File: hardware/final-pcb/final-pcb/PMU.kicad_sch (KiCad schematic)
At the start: 1 part, among them U3 LTC3556EUFD-PBF

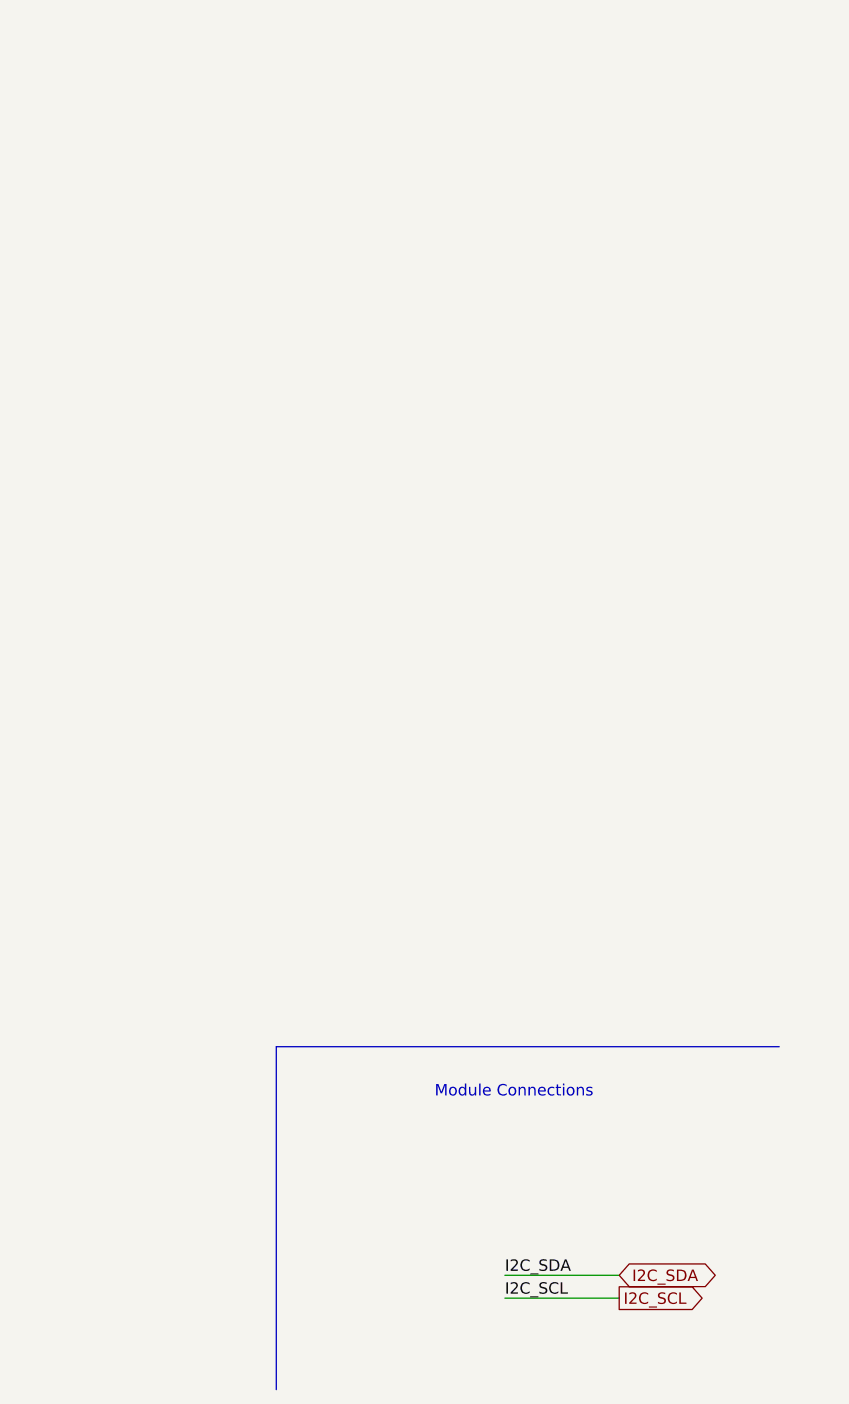
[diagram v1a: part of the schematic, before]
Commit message: Silkscreen board, add USB connector
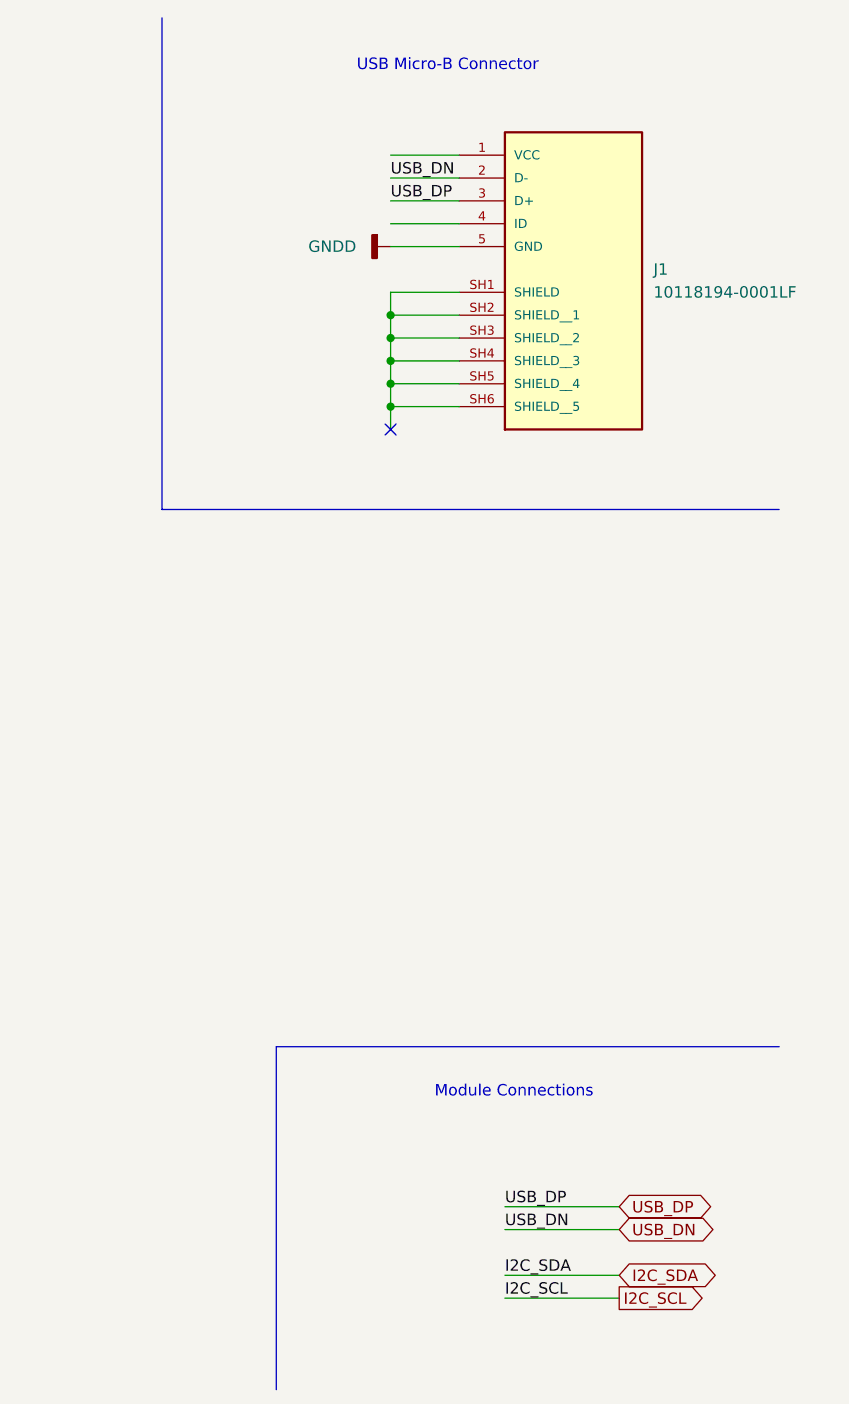
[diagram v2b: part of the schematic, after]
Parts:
- added J1: 10118194-0001LF, hands-emg-lib:10118194-0001LF, symbol hands-emg-lib:10118194-0001LF
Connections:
- new net: J1.SH1 (SHIELD), J1.SH2 (SHIELD__1), J1.SH3 (SHIELD__2), J1.SH4 (SHIELD__3), J1.SH5 (SHIELD__4), J1.SH6 (SHIELD__5)
- new net GNDD: J1.5 (GND)
- new net USB_DN: J1.2 (D-)
- new net USB_DP: J1.3 (D+)
- no-connect marks 0 -> 1
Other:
- note added: "USB Micro-B Connector"

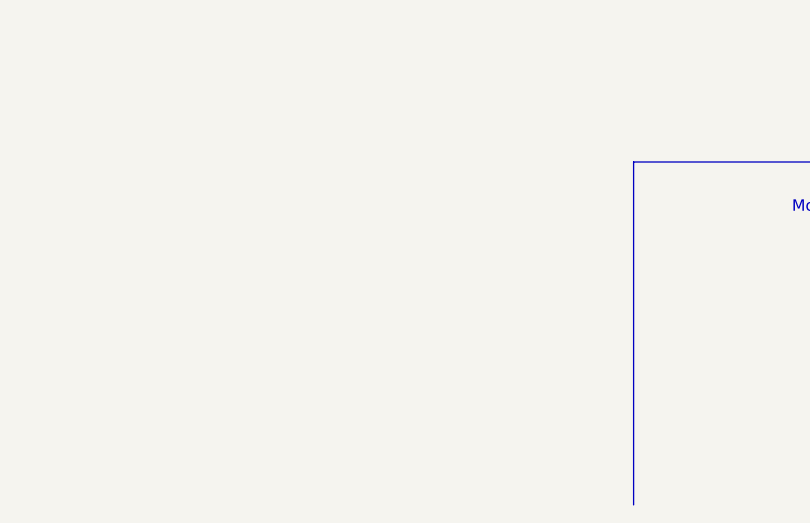
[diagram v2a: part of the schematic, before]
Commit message: Add syms, footprints, 3dmodels for ADS and LTC boards
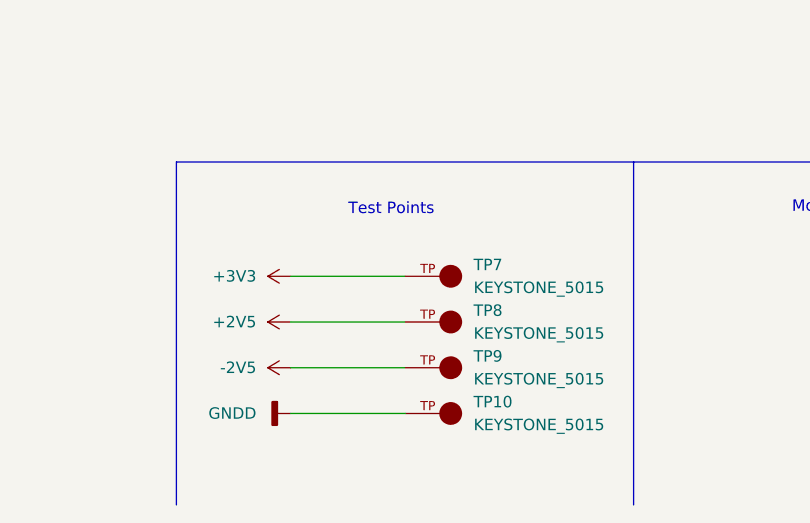
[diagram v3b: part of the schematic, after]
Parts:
- added TP10, TP7, TP8, TP9: KEYSTONE_5015, hands-emg-lib:KEYSTONE_5015, symbol hands-emg-lib:KEYSTONE_5015
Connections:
- net GNDD: now also TP10.TP
- new net +2V5: TP8.TP
- new net +3V3: TP7.TP
- new net -2V5: TP9.TP
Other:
- note added: "Test Points"
- company: (none) -> San Diego State University
- title: (none) -> Power Management Unit
